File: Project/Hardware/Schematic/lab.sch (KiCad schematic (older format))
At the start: 27 parts, among them J2 6P Male, U2 STM32F411RETx, Y1 8MHz

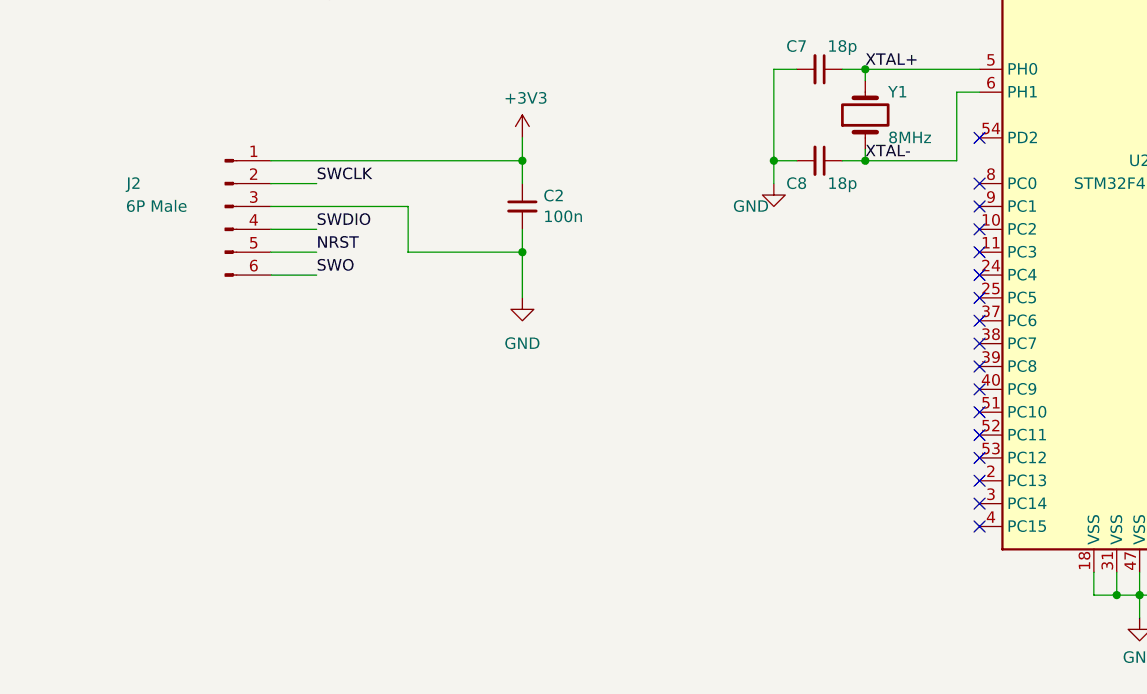
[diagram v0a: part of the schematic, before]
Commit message: La till connection stm32 till display, footprint for DEM16220 lcd
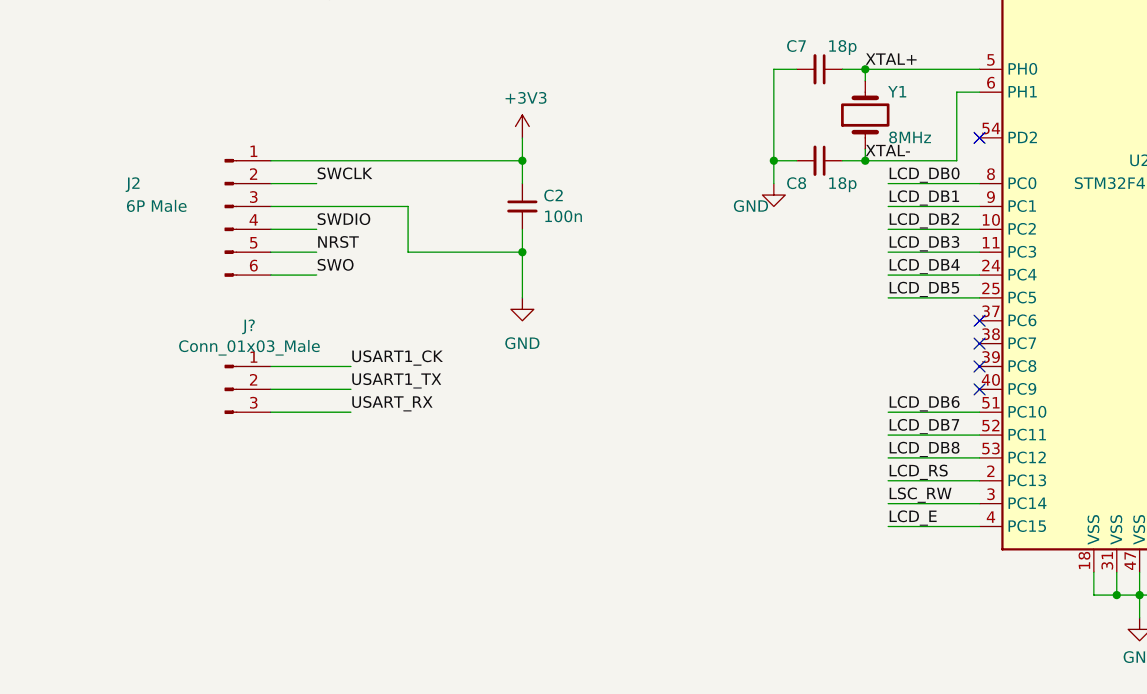
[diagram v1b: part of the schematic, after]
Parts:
- added J?: Conn_01x03_Male, symbol Connector:Conn_01x03_Male
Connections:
- net USART1_CK: now also J?.1 (Pin_1)
- net USART1_TX: now also J?.2 (Pin_2)
- net LCD_DB2: now reaches U2.10 (PC2)
- net LCD_DB3: now reaches U2.11 (PC3)
- net LCD_RS: now reaches U2.2 (PC13)
- net LCD_DB4: now reaches U2.24 (PC4)
- net LCD_DB5: now reaches U2.25 (PC5)
- net LSC_RW: now reaches U2.3 (PC14)
- net LCD_E: now reaches U2.4 (PC15)
- net LCD_DB6: now reaches U2.51 (PC10)
- net LCD_DB7: now reaches U2.52 (PC11)
- net LCD_DB8: now reaches U2.53 (PC12)
- net LCD_DB0: now reaches U2.8 (PC0)
- net LCD_DB1: now reaches U2.9 (PC1)
- new net USART_RX: J?.3 (Pin_3)
- no-connect marks 36 -> 24
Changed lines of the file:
@@
 NoConn ~ 7500 5700
 NoConn ~ 7500 5800
-NoConn ~ 6100 5800
-NoConn ~ 6100 5700
-NoConn ~ 6100 5600
-NoConn ~ 6100 5500
-NoConn ~ 6100 5400
-NoConn ~ 6100 5300
 NoConn ~ 6100 5200
 NoConn ~ 6100 5100
 NoConn ~ 6100 5000
 NoConn ~ 6100 4900
-NoConn ~ 6100 4800
-NoConn ~ 6100 4700
-NoConn ~ 6100 4600
-NoConn ~ 6100 4500
-NoConn ~ 6100 4400
-NoConn ~ 6100 4300
 NoConn ~ 6100 4100
 $Comp
@@
 Text Label 7900 3200 0    50   ~ 0
 TIM2_CH1
+$Comp
+L Connector:Conn_01x03_Male J?
+U 1 1 5C5B0DFA
+P 2800 5200
+F 0 "J?" H 2906 5478 50  0000 C CNN
+F 1 "Conn_01x03_Male" H 2906 5387 50  0000 C CNN
+F 2 "" H 2800 5200 50  0001 C CNN
+F 3 "~" H 2800 5200 50  0001 C CNN
+	1    2800 5200
+	1    0    0    -1
+$EndComp
+Wire Wire Line
+	3000 5100 3350 5100
+Text Label 3350 5100 0    50   ~ 0
+USART1_CK
+Wire Wire Line
+	3000 5200 3350 5200
+Text Label 3350 5200 0    50   ~ 0
+USART1_TX
+Wire Wire Line
+	3000 5300 3350 5300
+Text Label 3350 5300 0    50   ~ 0
+USART_RX
+Text Label 5700 4300 0    50   ~ 0
+LCD_DB0
+Text Label 5700 4400 0    50   ~ 0
+LCD_DB1
+Text Label 5700 4500 0    50   ~ 0
+LCD_DB2
+Wire Wire Line
+	5700 4300 6100 4300
+Wire Wire Line
+	5700 4400 6100 4400
+Wire Wire Line
+	5700 4500 6100 4500
+Wire Wire Line
+	6100 4600 5700 4600
+Text Label 5700 4600 0    50   ~ 0
+LCD_DB3
+Wire Wire Line
+	6100 4700 5700 4700
+Text Label 5700 4700 0    50   ~ 0
+LCD_DB4
+Wire Wire Line
+	6100 4800 5700 4800
+Text Label 5700 4800 0    50   ~ 0
+LCD_DB5
+Text Label 5700 5300 0    50   ~ 0
+LCD_DB6
+Text Label 5700 5400 0    50   ~ 0
+LCD_DB7
+Text Label 5700 5500 0    50   ~ 0
+LCD_DB8
+Wire Wire Line
+	5700 5300 6100 5300
+Wire Wire Line
+	5700 5400 6100 5400
+Wire Wire Line
+	5700 5500 6100 5500
+Wire Wire Line
+	6100 5600 5700 5600
+Text Label 5700 5600 0    50   ~ 0
+LCD_RS
+Wire Wire Line
+	6100 5700 5700 5700
+Text Label 5700 5700 0    50   ~ 0
+LSC_RW
+Wire Wire Line
+	6100 5800 5700 5800
+Text Label 5700 5800 0    50   ~ 0
+LCD_E
 $EndSCHEMATC

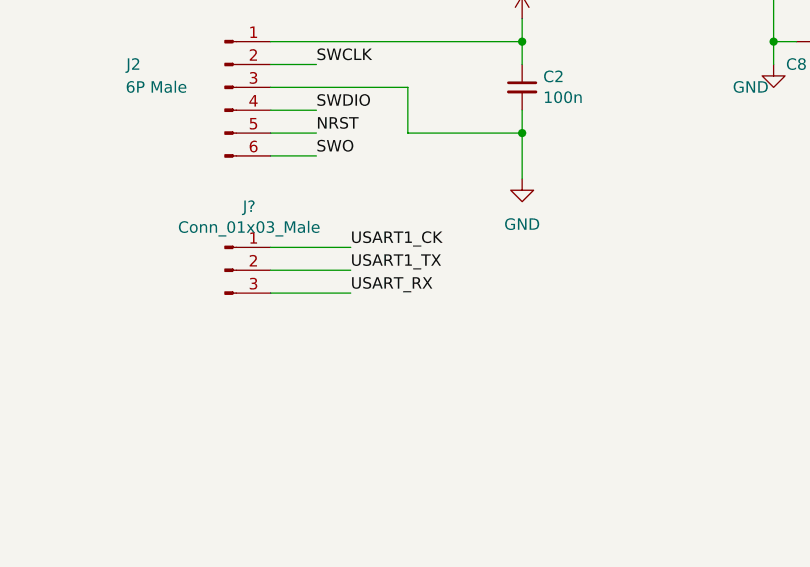
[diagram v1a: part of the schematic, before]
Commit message: Ändrade CS-pin på accelerometern, lade till kommentarer och värde på bypassen.
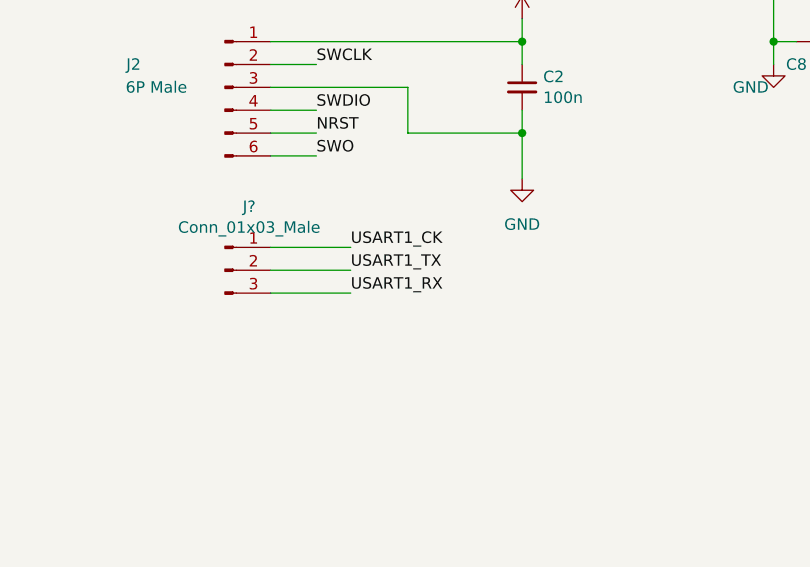
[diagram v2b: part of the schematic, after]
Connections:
- net USART_RX is gone; now on net USART1_RX: J?.3 (Pin_3)
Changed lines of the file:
@@
 	3000 5300 3350 5300
 Text Label 3350 5300 0    50   ~ 0
-USART_RX
+USART1_RX
 Text Label 5700 4300 0    50   ~ 0
 LCD_DB0
